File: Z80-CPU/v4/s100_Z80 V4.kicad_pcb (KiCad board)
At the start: 2 copper layers, 254 x 134.6 mm, 144 parts, among them K1 CONN_3, K17 EN_WAITS, K2 CONN_3, P1 S100_MALE, P2 CONN_4X2, P3 CLK_CPU, P34 CONN_1, P35 CONN_1, P36 CONN_3X2, P4 CONN_2X2, P5 XILINX CABLE2, P6 MASTER_OSC, P7 NMI, P8 CPLD Pins, Q1 NPN, Q2 NPN, Q3 NPN, SW1 RESET, SW2 DIPS_08, SW3 DIPS_08, SW4 DIPS_08, U1 Z80, U10 74LS165, U11 74LS165, U12 ^^74LS541, U13 2732, U14 74LS682N, U15 74LS153, U16 74LS153, U17 XC9572XL-TQ100, U18 74LS32, U19 74LS244, U2 ^^74LS541, U20 74LS244, U21 ^^74LS541, U22 ^^74LS541, U23 74LS02, U24 74LS04, U25 74LS04, U26 ^^LOGO1, U27 74LS139, U28 74LS00, U29 74LS273, U3 ^^74LS541, U30 74LS273, U31 74LS00, U32 74LS273, U33 74LS74, U34 74LS74, U36 74LS04, U37 74LS05, U39 74LS273, U4 74LS04, U40 74LS00, U45 74LS02, U48 LDO_REG_7805, U5 74LS157, U6 74LS157, U7 74LS32, U8 74LS157, U9 74LS165

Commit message: Z80-CPU v4: schematic and placement
Source: S100 Z80 version4/backups/28-06-2015 1855 (the same folder also exists, byte-identical, in S100 Z80 version5/backups)
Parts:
- removed JP1: JUMPER, PIN_ARRAY_2X1
- removed U17: XC9572XL-TQ100, XILINX-TQ100
- removed U24: 74LS04, DIP-14__300_ELL
- removed Ux1: ^^3.3VREG_SOT223, ^^SOT223v1
- added C6: 0.1 uF, C2, F.Cu at (95.5, 48.8)
- added IC1: XC9572PC84, XILINX-PLCC-S84, F.Cu at (57.3, 78.9)
- added P9: CONN_2, PIN_ARRAY_2X1, F.Cu at (76.8, 80.1)
- U13: footprint ^^DIP-24-ZIF -> -DIL24-6
- U18: footprint DIP-16__300_ELL -> DIP-14__300_ELL
- U23: footprint 14DIP-ELL300 -> DIP-14__300_ELL
- moved R19 203.8 mm to (247.0, 33.6), turned to 270 degrees
- moved SW1 203.8 mm to (247.0, 33.6)
- moved C54 88.3 mm to (36.3, 81.4)
- moved U31 47.5 mm to (171.4, 90.2)
- moved C49 38.1 mm to (21.8, 36.8)
- moved C12 38.1 mm to (51.8, 36.6)
- moved C4 38.1 mm to (51.8, 52.1)
- moved C59 38.1 mm to (21.8, 52.1)
- moved U15 38.1 mm to (35.7, 52.1)
- moved U16 38.1 mm to (65.9, 37.0)
- moved U23 38.1 mm to (34.4, 37.0)
- moved U5 38.1 mm to (65.9, 52.2)
- moved D10 30.7 mm to (104.8, 26.9)
- moved D7 30.7 mm to (98.2, 26.9)
- moved R16 30.7 mm to (98.2, 28.6)
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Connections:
- net /CPLD_P12 renamed /CPLD_P19
- net /CPLD_P94 renamed /CPLD_P44
- net /CPLD_P97 renamed /CPLD_P55
- net /CPLD_P99 renamed /CPLD_P66
- Cx2 pad 1: /V3.3 -> VCC
- D7 pad 1: /CPLD_P42 -> /CPLD_P81
- D9 pad 1: /CPLD_P49 -> /CPLD_P62
- P36 pad 3: /CPLD_P95 -> (no net)
- P5 pad 2: /V3.3 -> VCC
- P8 pad 1: N-00000210 (its old number) -> /CPLD_Pout1
- P8 pad 10: N-00000209 -> /CPLD_Pout10
- P8 pad 2: N-00000207 -> /CPLD_Pout2
- P8 pad 3: N-00000176 -> /CPLD_Pout3
- P8 pad 4: N-00000163 -> /CPLD_Pout4
- P8 pad 5: N-00000204 -> /CPLD_Pout5
- P8 pad 6: N-00000208 -> /CPLD_Pout6
- P8 pad 7: N-00000205 -> /CPLD_Pout7
- P8 pad 8: N-00000258 (its old number) -> /CPLD_Pout8
- P8 pad 9: N-00000206 -> /CPLD_Pout9
- R19 pad 1: /V3.3 -> VCC
- U1 pad 20: /CPLD_P8 -> /CPLD_P63
- U1 pad 21: /CPLD_P9 -> /CPLD_P72
- U1 pad 27: /CPLD_P10 -> /CPLD_P84
- U21 pad 3: /CPLD_P87 -> (no net)
- U21 pad 5: /CPLD_P91 -> (no net)
- U22 pad 2: N-00000403 -> N-00000426
- U22 pad 3: /CPLD_P16 -> (no net)
- U25 pad 5: (no net) -> N-00000431
- U25 pad 6: (no net) -> N-00000432
- U28 pad 6: N-00000421 (its old number) -> N-00000431
- U31 pad 10: /CPLD_P96 -> (no net)
- U31 pad 2: N-00000422 (its old number) -> N-00000432
- U36 pad 14: (no net) -> VCC
- U36 pad 7: (no net) -> GND
- U4 pad 14: (no net) -> VCC
- U4 pad 5: (no net) -> /HALT*
- U4 pad 6: (no net) -> N-00000426
- U4 pad 7: (no net) -> GND
- U7 pad 14: VCC -> (no net)
- U7 pad 7: GND -> (no net)
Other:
- net class Default: trace_width 0.24 -> 0.25
- net class Power: trace_width 0.6096 -> 0.75
- net class TempPWR added: clearance 0.2, trace_width 0.5, via_dia 0.5, via_drill 0.35
- net class gnd: trace_width 0.24 -> 0.25
- net class power8v: trace_width 1.2954 -> 2
- board text added: "NMI ENABLE"
- board text added: "OSC"
- board text removed: "MASTER OSC"

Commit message: Z80-CPU v4: routed trial
Source: S100 Z80 version4/backups/29-06-2015 morning (the same folder also exists, byte-identical, in S100 Z80 version5/backups)
Newest file is 2015-06-28 18:59.
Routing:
- net GND: track 0.00 -> 1636.6 mm, vias 0 -> 3
- net VCC: track 0.00 -> 1085.7 mm, vias 0 -> 1
- net /CPLD_P18: track 0.00 -> 361.9 mm, vias 0 -> 5
- net /bA5: track 0.00 -> 358.1 mm, vias 0 -> 3
- net /bA3: track 0.00 -> 353.4 mm, vias 0 -> 3
- net /bA4: track 0.00 -> 347.3 mm, vias 0 -> 7
- net /CPLD_P14: track 0.00 -> 346.2 mm, vias 0 -> 7
- net /D7: track 0.00 -> 343.0 mm, vias 0 -> 5
- net /D4: track 0.00 -> 335.1 mm, vias 0 -> 2
- net /D6: track 0.00 -> 330.4 mm, vias 0 -> 4
- net /D5: track 0.00 -> 328.4 mm, vias 0 -> 6
- net /bA6: track 0.00 -> 327.1 mm, vias 0 -> 7
- net /D3: track 0.00 -> 326.7 mm, vias 0 -> 2
- net /bA7: track 0.00 -> 324.6 mm, vias 0 -> 6
- net /bA2: track 0.00 -> 323.4 mm, vias 0 -> 5
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
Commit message: Z80-CPU v4: schematic and placement
Source: S100 Z80 version4/backups/29-06-2015 1549 (the same folder also exists, byte-identical, in S100 Z80 version5/backups)
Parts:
- added C7: 0.1 uF, C2, F.Cu at (77.7, 76.1)
- added P10: CONN_2, PIN_ARRAY_2X1, F.Cu at (32.8, 79.0)
- moved P9 2.88 mm to (79.7, 79.9)
- moved C54 0.13 mm to (36.3, 81.5)
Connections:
- C54 pad 1: VCC -> /V5.0temp
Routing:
- net GND: track 1636.6 -> 0.00 mm, vias 3 -> 0
- net VCC: track 1085.7 -> 0.00 mm, vias 1 -> 0
- net /CPLD_P18: track 361.9 -> 0.00 mm, vias 5 -> 0
- net /bA5: track 358.1 -> 0.00 mm, vias 3 -> 0
- net /bA3: track 353.4 -> 0.00 mm, vias 3 -> 0
- net /bA4: track 347.3 -> 0.00 mm, vias 7 -> 0
- net /CPLD_P14: track 346.2 -> 0.00 mm, vias 7 -> 0
- net /D7: track 343.0 -> 0.00 mm, vias 5 -> 0
- net /D4: track 335.1 -> 0.00 mm, vias 2 -> 0
- net /D6: track 330.4 -> 0.00 mm, vias 4 -> 0
- net /D5: track 328.4 -> 0.00 mm, vias 6 -> 0
- net /bA6: track 327.1 -> 0.00 mm, vias 7 -> 0
- net /D3: track 326.7 -> 0.00 mm, vias 2 -> 0
- net /bA7: track 324.6 -> 0.00 mm, vias 6 -> 0
- net /bA2: track 323.4 -> 0.00 mm, vias 5 -> 0
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
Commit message: Z80-CPU v4: schematic and routed trial
Source: S100 Z80 version4/backups/30-06-2015 morning (the same folder also exists, byte-identical, in S100 Z80 version5/backups)
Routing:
- net GND: track 0.00 -> 1656.6 mm, vias 0 -> 4
- net VCC: track 0.00 -> 1100.3 mm, vias 0 -> 3
- net /bA6: track 0.00 -> 355.0 mm, vias 0 -> 4
- net /bA3: track 0.00 -> 354.6 mm, vias 0 -> 3
- net /bA5: track 0.00 -> 352.8 mm, vias 0 -> 6
- net /bA4: track 0.00 -> 352.2 mm, vias 0 -> 6
- net /D6: track 0.00 -> 350.0 mm, vias 0 -> 6
- net /CPLD_P17: track 0.00 -> 341.1 mm, vias 0 -> 7
- net /D7: track 0.00 -> 331.6 mm, vias 0 -> 2
- net /D3: track 0.00 -> 325.6 mm, vias 0 -> 5
- net /CLK_CPU: track 0.00 -> 325.3 mm, vias 0 -> 7
- net /bA7: track 0.00 -> 323.1 mm, vias 0 -> 6
- net /D5: track 0.00 -> 322.1 mm, vias 0 -> 3
- net /bA2: track 0.00 -> 321.9 mm, vias 0 -> 5
- net /D2: track 0.00 -> 317.8 mm, vias 0 -> 5
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
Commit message: Z80-CPU v4: schematic, netlist and placement
Source: S100 Z80 version4/backups/30-06-2015 1801 (the same folder also exists, byte-identical, in S100 Z80 version5/backups)
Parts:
- added U17: 74LVC1G125, -SOT353, B.Cu at (42.0, 97.7)
- P8: footprint PIN_ARRAY_5x2 -> PIN_ARRAY_6x2
- moved P8 2.41 mm to (25.8, 67.8)
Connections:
- IC1 pad 2: (no net) -> /CPLD_P2
- IC1 pad 31: (no net) -> /CPLD_P31
- IC1 pad 32: (no net) -> /CPLD_P32
- IC1 pad 36: (no net) -> /CPLD_P36
- IC1 pad 43: (no net) -> /CPLD_P43
- IC1 pad 44: (no net) -> /CPLD_P44
- IC1 pad 46: (no net) -> /CPLD_P46
- IC1 pad 47: (no net) -> /CPLD_P47
- IC1 pad 51: (no net) -> /CPLD_P51
- IC1 pad 54: (no net) -> /CPLD_P54
- IC1 pad 55: (no net) -> /CPLD_P55
- IC1 pad 7: (no net) -> /CPLD_P7
- IC1 pad 71: (no net) -> /CPLD_P71
- IC1 pad 74: (no net) -> /CPLD_P74
- IC1 pad 76: (no net) -> /CPLD_P76
- IC1 pad 77: (no net) -> /CPLD_P77
- IC1 pad 80: (no net) -> /CPLD_P80
- IC1 pad 82: (no net) -> /CPLD_P82
- IC1 pad 83: (no net) -> /CPLD_P83
- P36 pad 3: (no net) -> /CPLD_P47
- R19 pad 2: /CPLD_P33 -> /CPLD_P76
- SW1 pad 2: /CPLD_P33 -> /CPLD_P76
- U1 pad 14: /D0 -> /CPLD_P33
- U1 pad 30: /bA0 -> /CPLD_P80
- U1 pad 31: /bA1 -> /CPLD_P83
- U1 pad 32: /bA2 -> /CPLD_P82
- U1 pad 33: /bA3 -> /CPLD_P7
- U1 pad 34: /bA4 -> /CPLD_P2
- U1 pad 35: /bA5 -> /CPLD_P43
- U1 pad 36: /bA6 -> /CPLD_P36
- U1 pad 37: /bA7 -> /CPLD_P71
- U13 pad 1: /bA7 -> /CPLD_P71
- U13 pad 2: /bA6 -> /CPLD_P36
- U13 pad 3: /bA5 -> /CPLD_P43
- U13 pad 4: /bA4 -> /CPLD_P2
- U13 pad 5: /bA3 -> /CPLD_P7
- U13 pad 6: /bA2 -> /CPLD_P82
- U13 pad 7: /bA1 -> /CPLD_P83
- U13 pad 8: /bA0 -> /CPLD_P80
- U13 pad 9: /D0 -> /CPLD_P33
- U14 pad 11: /bA4 -> /CPLD_P2
- U14 pad 13: /bA5 -> /CPLD_P43
- U14 pad 15: /bA6 -> /CPLD_P36
- U14 pad 17: /bA7 -> /CPLD_P71
- U14 pad 6: /bA2 -> /CPLD_P82
- U14 pad 8: /bA3 -> /CPLD_P7
- U19 pad 17: /D0 -> /CPLD_P33
- U2 pad 2: /bA7 -> /CPLD_P71
- U2 pad 3: /bA6 -> /CPLD_P36
- U2 pad 4: /bA5 -> /CPLD_P43
- U2 pad 5: /bA4 -> /CPLD_P2
- U2 pad 6: /bA3 -> /CPLD_P7
- U2 pad 7: /bA2 -> /CPLD_P82
- U2 pad 8: /bA1 -> /CPLD_P83
- U2 pad 9: /bA0 -> /CPLD_P80
- U20 pad 3: /D0 -> /CPLD_P33
- U21 pad 3: (no net) -> /CPLD_P46
- U21 pad 5: (no net) -> /CPLD_P51
- U27 pad 2: /bA0 -> /CPLD_P80
- U27 pad 3: /bA1 -> /CPLD_P83
- U29 pad 18: /D0 -> /CPLD_P33
- U30 pad 18: /D0 -> /CPLD_P33
- U31 pad 10: (no net) -> /CPLD_P54
- U32 pad 18: /D0 -> /CPLD_P33
- U39 pad 18: /D0 -> /CPLD_P33
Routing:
- net GND: track 1656.6 -> 0.00 mm, vias 4 -> 0
- net VCC: track 1100.3 -> 0.00 mm, vias 3 -> 0
- net /bA6: track 355.0 -> 0.00 mm, vias 4 -> 0
- net /bA3: track 354.6 -> 0.00 mm, vias 3 -> 0
- net /bA5: track 352.8 -> 0.00 mm, vias 6 -> 0
- net /bA4: track 352.2 -> 0.00 mm, vias 6 -> 0
- net /D6: track 350.0 -> 0.00 mm, vias 6 -> 0
- net /CPLD_P17: track 341.1 -> 0.00 mm, vias 7 -> 0
- net /D7: track 331.6 -> 0.00 mm, vias 2 -> 0
- net /D3: track 325.6 -> 0.00 mm, vias 5 -> 0
- net /CLK_CPU: track 325.3 -> 0.00 mm, vias 7 -> 0
- net /bA7: track 323.1 -> 0.00 mm, vias 6 -> 0
- net /D5: track 322.1 -> 0.00 mm, vias 3 -> 0
- net /bA2: track 321.9 -> 0.00 mm, vias 5 -> 0
- net /D2: track 317.8 -> 0.00 mm, vias 5 -> 0
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
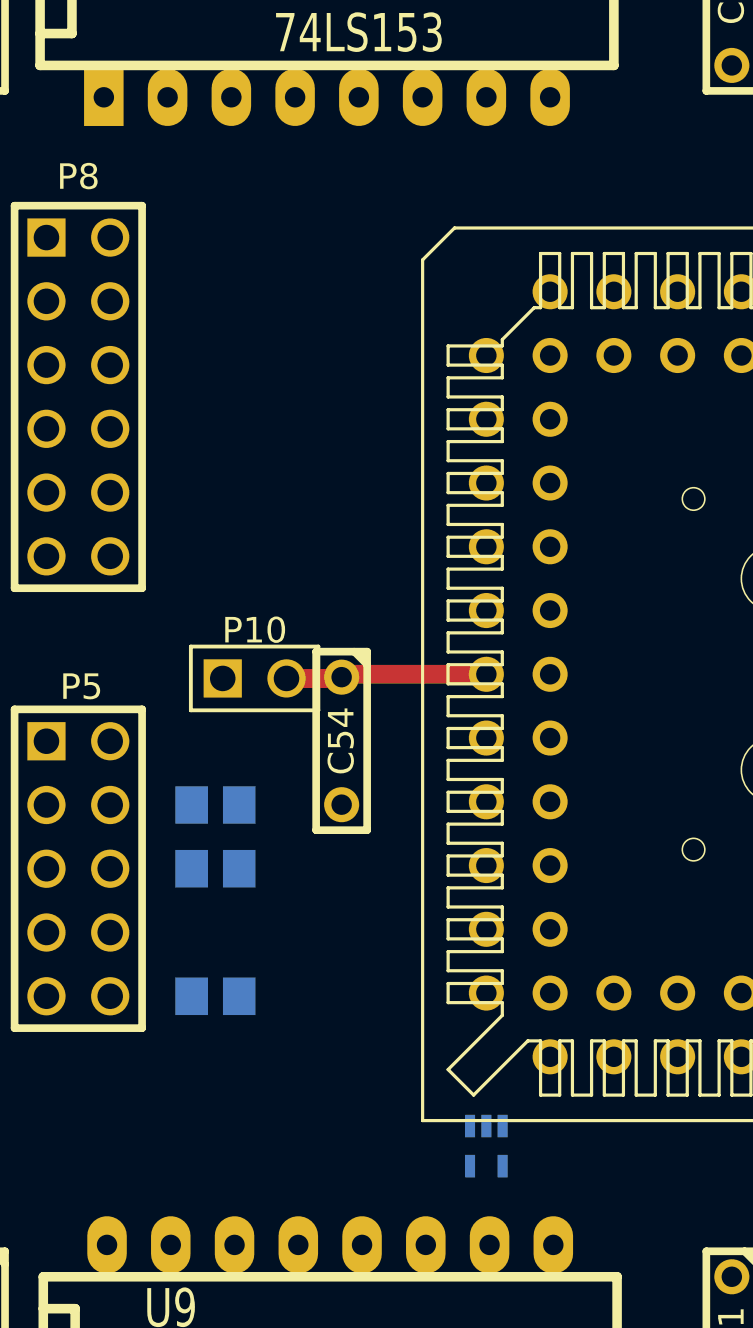
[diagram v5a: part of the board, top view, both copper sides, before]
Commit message: Z80-CPU v4: schematic, placement and IC parts list
Source: S100 Z80 version4/backups/02-07-215 1901 (the same folder also exists, byte-identical, in S100 Z80 version5/backups) (folder name has a year typo: 215).
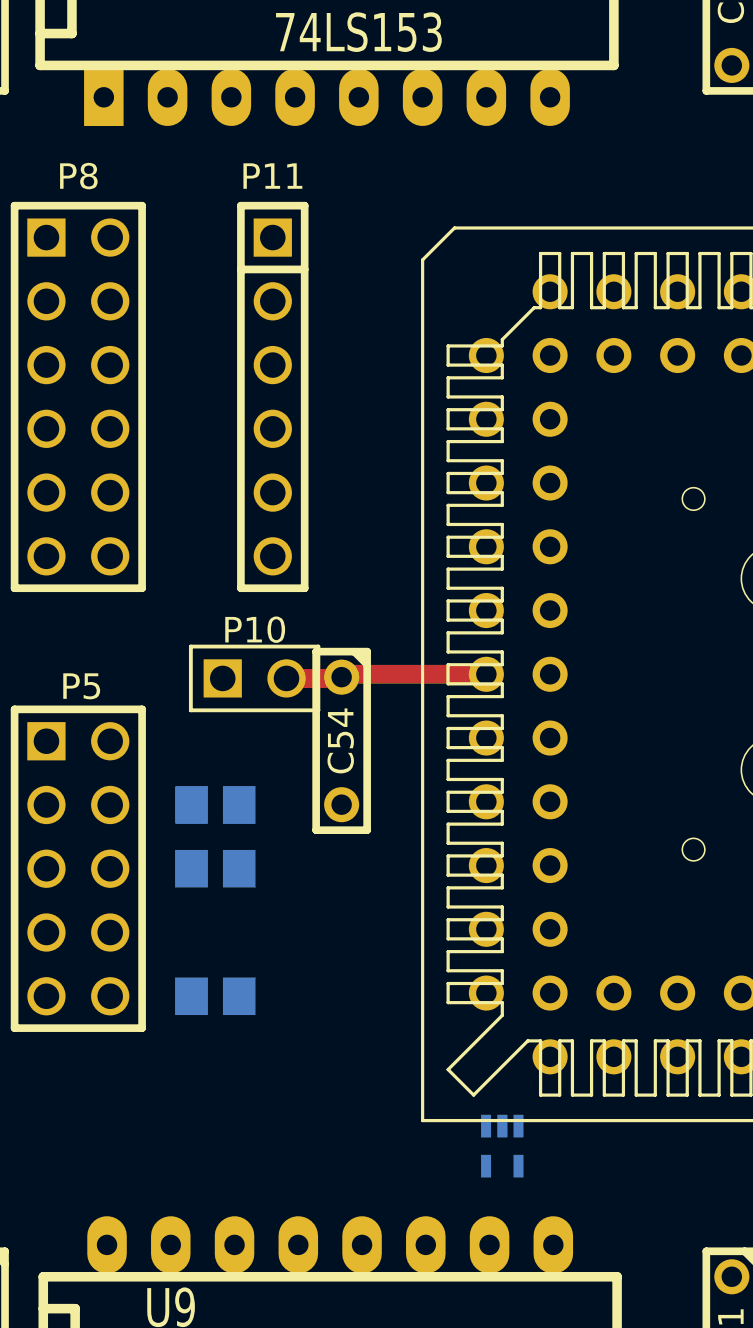
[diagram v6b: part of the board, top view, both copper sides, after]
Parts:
- added P11: CONN_6, PIN_ARRAY_6X1, F.Cu at (33.5, 67.8)
- moved U17 0.63 mm to (42.7, 97.7)
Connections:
- IC1 pad 3: (no net) -> /CPLD_P3
- IC1 pad 4: (no net) -> /CPLD_P4
- IC1 pad 48: (no net) -> /CPLD_P48
- IC1 pad 52: (no net) -> /CPLD_P52
- IC1 pad 69: (no net) -> /CPLD_P69
- IC1 pad 75: (no net) -> /CPLD_P75
- IC1 pad 79: (no net) -> /CPLD_P79
- P6 pad 2: /CLK_CPU -> N-00000424
- P6 pad 4: /CLK_CPU -> N-00000424
- P8 pad 12: /CPLD_P77 -> GND
- U1 pad 6: (no net) -> /CLK_CPU
- U21 pad 8: (no net) -> /CPLD_P69
- U22 pad 3: (no net) -> /CPLD_P48
- U25 pad 10: (no net) -> N-00000204
- U25 pad 11: (no net) -> N-00000424
- U25 pad 8: (no net) -> /CLK_CPU
- U25 pad 9: (no net) -> N-00000204
- U28 pad 1: (no net) -> /CPLD_P52

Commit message: Z80-CPU v4: routed REV 4.0 board and gerbers sent to PCBway
Source: S100 Z80 version4/GERBERS (an identical copy is in GERBERS/SENT to PCBway 28-07-2015) and S100 Z80 version4/s100_Z80 V4.kicad_pcb-bak.
The routed board at gerber time (2015-07-28 09:27) survives as s100_Z80 V4.kicad_pcb-bak; it is committed as s100_Z80 V4.kicad_pcb.
The .drl was re-exported from gerbv as RS-274X at 14:41.
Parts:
- removed P10, P9: CONN_2, PIN_ARRAY_2X1
- IC1: footprint XILINX-PLCC-S84 -> ^^XILINX-PLCC-S84
- U13: footprint -DIL24-6 -> ^^DIL24-6
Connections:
- C54 pad 1: /V5.0temp -> VCC
- C7 pad 1: /V5.0temp -> VCC
- IC1 pad 22: /V5.0temp -> VCC
- IC1 pad 38: /V5.0temp -> VCC
- IC1 pad 64: /V5.0temp -> VCC
- IC1 pad 73: /V5.0temp -> VCC
- IC1 pad 78: /V5.0temp -> VCC
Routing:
- net GND: track 0.00 -> 2078.2 mm, vias 0 -> 80
- net VCC: track 0.00 -> 1207.9 mm, vias 0 -> 5
- net /CPLD_P82: track 0.00 -> 430.2 mm, vias 0 -> 4
- net /CPLD_P2: track 0.00 -> 415.5 mm, vias 0 -> 4
- net /CPLD_P33: track 0.00 -> 402.6 mm, vias 0 -> 8
- net /CPLD_P43: track 0.00 -> 395.9 mm, vias 0 -> 3
- net /CPLD_P7: track 0.00 -> 382.0 mm, vias 0 -> 7
- net /CLK_CPU: track 0.00 -> 372.3 mm, vias 0 -> 5
- net /CPLD_P20: track 0.00 -> 368.7 mm, vias 0 -> 3
- net /CPLD_P36: track 0.00 -> 368.2 mm, vias 0 -> 8
- net /CPLD_P71: track 0.00 -> 362.6 mm, vias 0 -> 7
- net /CPLD_P13: track 0.00 -> 362.1 mm, vias 0 -> 2
- net /CPLD_P18: track 0.00 -> 362.0 mm, vias 0 -> 3
- net /D6: track 0.00 -> 347.2 mm, vias 0 -> 8
- net /D5: track 0.00 -> 334.2 mm, vias 0 -> 5
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- added copper zone on B.Cu, net GND
- added copper zone on F.Cu, net GND
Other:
- board text added: "GND P75 P79 P4 P77 P3"
- board text added: "IC1"
- board text added: "R7"
- board text added: "U10"
- board text added: "U11"
- board text added: "U12"
- board text added: "U13"
- board text added: "U14"
- board text added: "U15"
- board text added: "U16"
- board text added: "U18"
- board text added: "U19"
- board text added: "U2"
- board text added: "U20"
- board text added: "U21"
- board text added: "U22"
- board text added: "U23"
- board text added: "U27"
- board text added: "U28"
- board text added: "U29"
- board text added: "U3"
- board text added: "U30"
- board text added: "U31"
- board text added: "U32"
- board text added: "U33"
- board text added: "U34"
- board text added: "U36"
- board text added: "U37"
- board text added: "U39"
- board text added: "U4"
- board text added: "U40"
- board text added: "U45"
- board text added: "U5"
- board text added: "U6"
- board text added: "U7"
- board text added: "U8"
- board text added: "U9"
- board text added: "XC9572PC84"
- board text added: "Z80 CPU - REV 4.0 © 2015 A Burrows"
